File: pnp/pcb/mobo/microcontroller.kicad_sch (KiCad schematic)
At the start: 56 parts, among them J11 XY_LIMIT, J13 HOST, J14 HACK_HEADER, J15 FAN, J17 Z_LIMIT, J2 SWD Header, Q5 AO3400A, Q6 AO3400A, SW1 SW_Push, SW2 SW_Push, U1 STM32F407VETx, U23 PESD5V2S2UT, U24 PESD3V3S2UT, U25 PESD3V3S2UT, U26 PESD3V3S2UT, U27 PESD3V3S2UT, Y1 8MHz

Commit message: Capacitor sourcing
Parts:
- C1, C3, C6, C7: value 2u2 -> 2.2u; JLCPCB C49217 -> C377773; LCSC C49217 -> C377773
- C1, C16, C17, C23: LCSC C476766 -> C38141
- C10, C11, C12, C5, C8, C9: LCSC C360619 -> C38141
- C2, C4: JLCPCB C1785 -> C157608; LCSC C525280 -> C157608
- C29: LCSC C476766 -> C38141; now not fitted
- J11: JLCPCB (none) -> C67258; LCSC (none) -> C67258
- J15: JLCPCB (none) -> C64658; LCSC (none) -> C64658
- J2: now not fitted
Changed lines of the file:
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@@
 			(effects
 				(font
-					(size 1 1)
-					(color 223 129 255 1)
+					(size 1.27 1.27)
 				)
 				(hide yes)
@@
 			(effects
 				(font
-					(size 1 1)
-					(color 223 129 255 1)
+					(size 1.27 1.27)
 				)
 				(hide yes)
 			)
 		)
-		(property "Description" ""
+		(property "Description" "test point"
 			(at 199.39 76.2 0)
 			(effects
@@
 			)
 		)
-		(property "LCSC" "C476766"
+		(property "LCSC" "C38141"
 			(at 146.05 77.47 0)
 			(effects
@@
 			)
 		)
-		(property "LCSC" "C360619"
+		(property "LCSC" "C38141"
 			(at 205.74 39.37 0)
 			(effects
@@
 			)
 		)
-		(property "Value" "2u2"
+		(property "Value" "2.2u"
 			(at 162.56 41.91 0)
 			(effects
@@
 			)
 		)
-		(property "JLCPCB" "C49217"
+		(property "JLCPCB" "C377773"
 			(at 161.29 39.37 0)
 			(effects
@@
 			)
 		)
-		(property "LCSC" "C49217"
+		(property "LCSC" "C377773"
 			(at 161.29 39.37 0)
 			(effects
@@
 			)
 		)
-		(property "LCSC" "C476766"
+		(property "LCSC" "C38141"
 			(at 149.225 254.635 0)
 			(effects
@@
 			)
 		)
-		(property "LCSC" "C360619"
+		(property "LCSC" "C38141"
 			(at 223.52 39.37 0)
 			(effects
@@
 			)
 		)
-		(property "Value" "2u2"
+		(property "Value" "2.2u"
 			(at 171.45 41.91 0)
 			(effects
@@
 			)
 		)
-		(property "JLCPCB" "C49217"
+		(property "JLCPCB" "C377773"
 			(at 170.18 39.37 0)
 			(effects
@@
 			)
 		)
-		(property "LCSC" "C49217"
+		(property "LCSC" "C377773"
 			(at 170.18 39.37 0)
 			(effects
@@
 		(in_bom yes)
 		(on_board yes)
-		(dnp no)
+		(dnp yes)
 		(property "Reference" "J2"
 			(at 158.75 123.19 0)
@@
 			(effects
 				(font
-					(size 1 1)
-					(color 223 129 255 1)
+					(size 1.27 1.27)
 				)
 				(hide yes)
@@
 			(effects
 				(font
-					(size 1 1)
-					(color 223 129 255 1)
+					(size 1.27 1.27)
 				)
 				(hide yes)
 			)
 		)
-		(property "Description" ""
+		(property "Description" "test point"
 			(at 152.4 71.12 0)
 			(effects
@@
 			)
 		)
-		(property "LCSC" "C476766"
+		(property "LCSC" "C38141"
 			(at 89.535 255.27 0)
 			(effects
@@
 			)
 		)
+		(property "JLCPCB" "C64658"
+			(at 391.795 208.28 0)
+			(effects
+				(font
+					(size 1.27 1.27)
+				)
+				(hide yes)
+			)
+		)
+		(property "LCSC" "C64658"
+			(at 391.795 208.28 0)
+			(effects
+				(font
+					(size 1.27 1.27)
+				)
+				(hide yes)
+			)
+		)
 		(pin "1"
 		)
@@
 			)
 		)
-		(property "LCSC" "C360619"
+		(property "LCSC" "C38141"
 			(at 196.85 39.37 0)
 			(effects
@@
 			)
 		)
-		(property "JLCPCB" "C1785"
+		(property "JLCPCB" "C157608"
 			(at 30.48 92.71 0)
 			(effects
@@
 			)
 		)
-		(property "LCSC" "C525280"
+		(property "LCSC" "C157608"
 			(at 30.48 92.71 0)
 			(effects
@@
 			)
 		)
-		(property "JLCPCB" "C1785"
+		(property "JLCPCB" "C157608"
 			(at 50.8 92.71 0)
 			(effects
@@
 			)
 		)
-		(property "LCSC" "C525280"
+		(property "LCSC" "C157608"
 			(at 50.8 92.71 0)
 			(effects
@@
 			)
 		)
-		(property "LCSC" "C360619"
+		(property "LCSC" "C38141"
 			(at 214.63 39.37 0)
 			(effects
@@
 			)
 		)
-		(property "Value" "2u2"
+		(property "Value" "2.2u"
 			(at 36.83 67.31 0)
 			(effects
@@
 			)
 		)
-		(property "JLCPCB" "C49217"
+		(property "JLCPCB" "C377773"
 			(at 41.91 64.77 0)
 			(effects
@@
 			)
 		)
-		(property "LCSC" "C49217"
+		(property "LCSC" "C377773"
 			(at 41.91 64.77 0)
 			(effects
@@
 		(in_bom yes)
 		(on_board yes)
-		(dnp no)
+		(dnp yes)
 		(property "Reference" "C29"
 			(at 201.7268 78.8416 0)
@@
 			)
 		)
-		(property "LCSC" "C476766"
+		(property "LCSC" "C38141"
 			(at 199.39 80.01 0)
 			(effects
@@
 			)
 		)
-		(property "LCSC" "C360619"
+		(property "LCSC" "C38141"
 			(at 179.07 39.37 0)
 			(effects
@@
 			)
 		)
-		(property "LCSC" "C360619"
+		(property "LCSC" "C38141"
 			(at 187.96 39.37 0)
 			(effects
@@
 			)
 		)
-		(property "Value" "2u2"
+		(property "Value" "2.2u"
 			(at 46.99 67.31 0)
 			(effects
@@
 			)
 		)
-		(property "JLCPCB" "C49217"
+		(property "JLCPCB" "C377773"
 			(at 52.07 64.77 0)
 			(effects
@@
 			)
 		)
-		(property "LCSC" "C49217"
+		(property "LCSC" "C377773"
 			(at 52.07 64.77 0)
 			(effects
@@
 			)
 		)
-		(property "LCSC" "C476766"
+		(property "LCSC" "C38141"
 			(at 120.015 254.635 0)
 			(effects
@@
 			(effects
 				(font
-					(size 1 1)
-					(color 223 129 255 1)
+					(size 1.27 1.27)
 				)
 				(hide yes)
@@
 			(effects
 				(font
-					(size 1 1)
-					(color 223 129 255 1)
+					(size 1.27 1.27)
 				)
 				(hide yes)
 			)
 		)
-		(property "Description" ""
+		(property "Description" "test point"
 			(at 189.23 134.62 0)
 			(effects
@@
 			)
 		)
+		(property "JLCPCB" "C67258"
+			(at 139.7 225.425 0)
+			(effects
+				(font
+					(size 1.27 1.27)
+				)
+				(hide yes)
+			)
+		)
+		(property "LCSC" "C67258"
+			(at 139.7 225.425 0)
+			(effects
+				(font
+					(size 1.27 1.27)
+				)
+				(hide yes)
+			)
+		)
 		(pin "2"
 		)
@@
 			(effects
 				(font
-					(size 1 1)
-					(color 223 129 255 1)
+					(size 1.27 1.27)
 				)
 				(hide yes)
@@
 			(effects
 				(font
-					(size 1 1)
-					(color 223 129 255 1)
+					(size 1.27 1.27)
 				)
 				(hide yes)
 			)
 		)
-		(property "Description" ""
+		(property "Description" "test point"
 			(at 189.23 137.16 0)
 			(effects

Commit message: Sourcing complete
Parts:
- J11: LCSC C67258 -> C2829152
- J13: JLCPCB (none) -> C2829154; LCSC (none) -> C64659
- J14: now not fitted
- J15: LCSC C64658 -> C2829150
- J17: JLCPCB (none) -> C146056; LCSC (none) -> C2829153
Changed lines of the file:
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@@
 			)
 		)
+		(property "JLCPCB" "C2829154"
+			(at 29.21 224.79 0)
+			(effects
+				(font
+					(size 1.27 1.27)
+				)
+				(hide yes)
+			)
+		)
+		(property "LCSC" "C64659"
+			(at 29.21 224.79 0)
+			(effects
+				(font
+					(size 1.27 1.27)
+				)
+				(hide yes)
+			)
+		)
 		(pin "3"
 		)
@@
 		(in_bom yes)
 		(on_board yes)
-		(dnp no)
+		(dnp yes)
 		(fields_autoplaced yes)
 		(property "Reference" "J14"
@@
 			)
 		)
-		(property "LCSC" "C64658"
+		(property "LCSC" "C2829150"
 			(at 391.795 208.28 0)
 			(effects
@@
 			)
 		)
+		(property "JLCPCB" "C146056"
+			(at 110.49 223.52 0)
+			(effects
+				(font
+					(size 1.27 1.27)
+				)
+				(hide yes)
+			)
+		)
+		(property "LCSC" "C2829153"
+			(at 110.49 223.52 0)
+			(effects
+				(font
+					(size 1.27 1.27)
+				)
+				(hide yes)
+			)
+		)
 		(pin "MP"
 		)
@@
 			)
 		)
-		(property "LCSC" "C67258"
+		(property "LCSC" "C2829152"
 			(at 139.7 225.425 0)
 			(effects

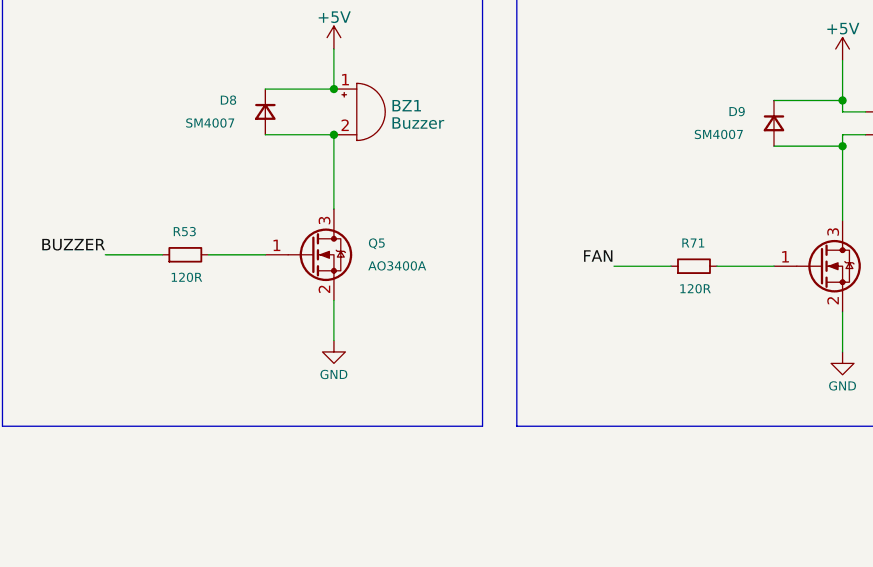
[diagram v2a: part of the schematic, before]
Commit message: Sourcing of resistors complete
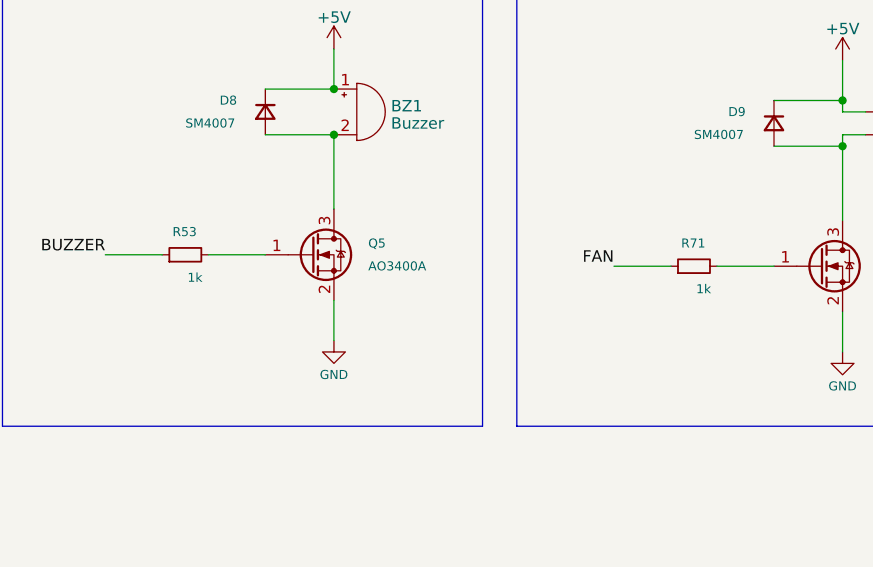
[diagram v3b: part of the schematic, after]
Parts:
- R11, R13, R14: LCSC C17414 -> C115295
- R53, R71: value 120R -> 1k; JLCPCB C17414 -> C17513; LCSC C17414 -> C17513
- R54, R55, R56, R8: JLCPCB C17414 -> C25275; LCSC C17414 -> C25275
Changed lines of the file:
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@@
 			)
 		)
-		(property "LCSC" "C17414"
+		(property "LCSC" "C115295"
 			(at 191.77 80.01 0)
 			(effects
@@
 			)
 		)
-		(property "Value" "120R"
+		(property "Value" "1k"
 			(at 369.57 227.965 90)
 			(effects
@@
 			)
 		)
-		(property "JLCPCB" "C17414"
+		(property "JLCPCB" "C17513"
 			(at 367.665 225.425 0)
 			(effects
@@
 			)
 		)
-		(property "LCSC" "C17414"
+		(property "LCSC" "C17513"
 			(at 367.665 225.425 0)
 			(effects
@@
 			)
 		)
-		(property "JLCPCB" "C17414"
+		(property "JLCPCB" "C25275"
 			(at 363.22 50.8 0)
 			(effects
@@
 			)
 		)
-		(property "LCSC" "C17414"
+		(property "LCSC" "C25275"
 			(at 363.22 50.8 0)
 			(effects
@@
 			)
 		)
-		(property "JLCPCB" "C17414"
+		(property "JLCPCB" "C25275"
 			(at 347.345 44.45 0)
 			(effects
@@
 			)
 		)
-		(property "LCSC" "C17414"
+		(property "LCSC" "C25275"
 			(at 347.345 44.45 0)
 			(effects
@@
 			)
 		)
-		(property "LCSC" "C17414"
+		(property "LCSC" "C115295"
 			(at 177.8 80.01 0)
 			(effects
@@
 			)
 		)
-		(property "LCSC" "C17414"
+		(property "LCSC" "C115295"
 			(at 146.05 67.31 0)
 			(effects
@@
 			)
 		)
-		(property "JLCPCB" "C17414"
+		(property "JLCPCB" "C25275"
 			(at 370.84 53.975 0)
 			(effects
@@
 			)
 		)
-		(property "LCSC" "C17414"
+		(property "LCSC" "C25275"
 			(at 370.84 53.975 0)
 			(effects
@@
 			)
 		)
-		(property "Value" "120R"
+		(property "Value" "1k"
 			(at 313.055 226.695 90)
 			(effects
@@
 			)
 		)
-		(property "JLCPCB" "C17414"
+		(property "JLCPCB" "C17513"
 			(at 311.15 224.155 0)
 			(effects
@@
 			)
 		)
-		(property "LCSC" "C17414"
+		(property "LCSC" "C17513"
 			(at 311.15 224.155 0)
 			(effects
@@
 			)
 		)
-		(property "JLCPCB" "C17414"
+		(property "JLCPCB" "C25275"
 			(at 355.6 47.625 0)
 			(effects
@@
 			)
 		)
-		(property "LCSC" "C17414"
+		(property "LCSC" "C25275"
 			(at 355.6 47.625 0)
 			(effects

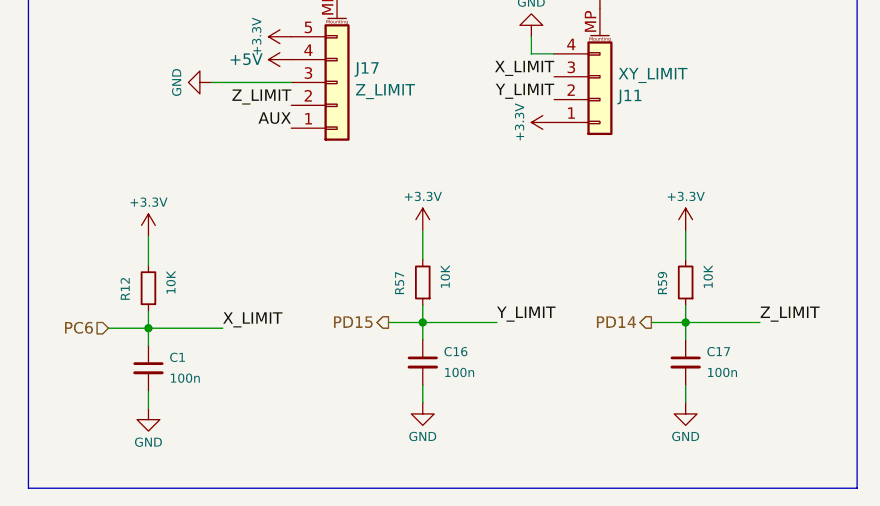
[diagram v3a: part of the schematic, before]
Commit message: Fix part sourcing
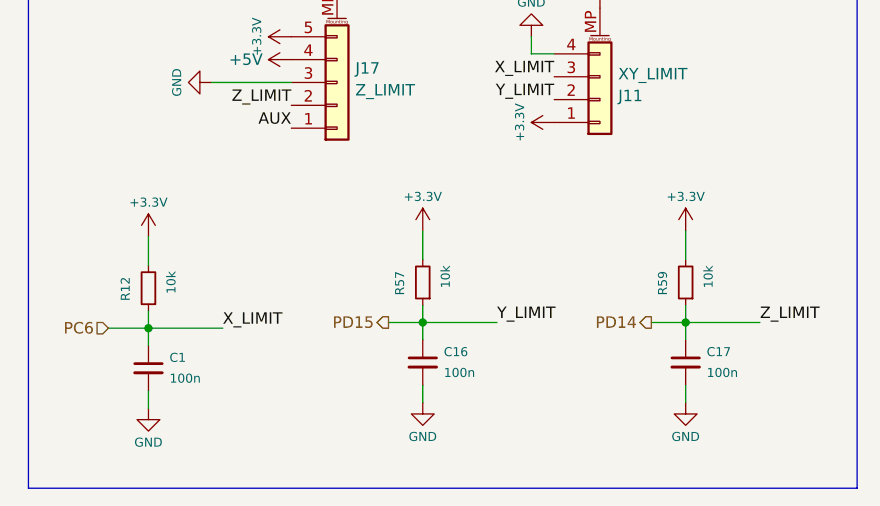
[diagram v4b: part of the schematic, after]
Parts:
- R12, R57, R59: value 10K -> 10k; LCSC C17414 -> C115295
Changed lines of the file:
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@@
 			)
 		)
-		(property "Value" "10K"
+		(property "Value" "10k"
 			(at 151.765 243.84 90)
 			(effects
@@
 			)
 		)
-		(property "LCSC" "C17414"
+		(property "LCSC" "C115295"
 			(at 149.225 245.745 0)
 			(effects
@@
 			)
 		)
-		(property "Value" "10K"
+		(property "Value" "10k"
 			(at 122.555 243.84 90)
 			(effects
@@
 			)
 		)
-		(property "LCSC" "C17414"
+		(property "LCSC" "C115295"
 			(at 120.015 245.745 0)
 			(effects
@@
 			)
 		)
-		(property "Value" "10K"
+		(property "Value" "10k"
 			(at 92.075 244.475 90)
 			(effects
@@
 			)
 		)
-		(property "LCSC" "C17414"
+		(property "LCSC" "C115295"
 			(at 89.535 246.38 0)
 			(effects

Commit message: Change Button PN
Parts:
- SW1, SW2: JLCPCB C720477 -> C455108; LCSC C720477 -> C455108
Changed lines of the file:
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@@
 			)
 		)
-		(property "JLCPCB" "C720477"
+		(property "JLCPCB" "C455108"
 			(at 152.4 77.47 0)
 			(effects
@@
 			)
 		)
-		(property "LCSC" "C720477"
+		(property "LCSC" "C455108"
 			(at 152.4 77.47 0)
 			(effects
@@
 			)
 		)
-		(property "JLCPCB" "C720477"
+		(property "JLCPCB" "C455108"
 			(at 191.77 69.85 0)
 			(effects
@@
 			)
 		)
-		(property "LCSC" "C720477"
+		(property "LCSC" "C455108"
 			(at 191.77 69.85 0)
 			(effects

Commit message: Sourcing of ESD dodes
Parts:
- BZ1: JLCPCB (none) -> C18623826; LCSC (none) -> C18623826
- J14: JLCPCB (none) -> C5383105; LCSC (none) -> C5383105
- U23: JLCPCB (none) -> C2827690; LCSC (none) -> C2827690
- U24, U25, U26, U27: JLCPCB (none) -> C84276; LCSC (none) -> C84276
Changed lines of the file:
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@@
 			)
 		)
+		(property "JLCPCB" "C2827690"
+			(at 328.93 116.205 0)
+			(effects
+				(font
+					(size 1.27 1.27)
+				)
+				(hide yes)
+			)
+		)
+		(property "LCSC" "C2827690"
+			(at 328.93 116.205 0)
+			(effects
+				(font
+					(size 1.27 1.27)
+				)
+				(hide yes)
+			)
+		)
 		(pin "1"
 		)
@@
 			)
 		)
+		(property "JLCPCB" "C84276"
+			(at 358.14 147.32 0)
+			(effects
+				(font
+					(size 1.27 1.27)
+				)
+				(hide yes)
+			)
+		)
+		(property "LCSC" "C84276"
+			(at 358.14 147.32 0)
+			(effects
+				(font
+					(size 1.27 1.27)
+				)
+				(hide yes)
+			)
+		)
 		(pin "1"
 		)
@@
 			)
 		)
+		(property "JLCPCB" "C5383105"
+			(at 225.425 257.175 0)
+			(effects
+				(font
+					(size 1.27 1.27)
+				)
+				(hide yes)
+			)
+		)
+		(property "LCSC" "C5383105"
+			(at 225.425 257.175 0)
+			(effects
+				(font
+					(size 1.27 1.27)
+				)
+				(hide yes)
+			)
+		)
 		(pin "1"
 		)
@@
 			)
 		)
+		(property "JLCPCB" "C84276"
+			(at 358.775 116.205 0)
+			(effects
+				(font
+					(size 1.27 1.27)
+				)
+				(hide yes)
+			)
+		)
+		(property "LCSC" "C84276"
+			(at 358.775 116.205 0)
+			(effects
+				(font
+					(size 1.27 1.27)
+				)
+				(hide yes)
+			)
+		)
 		(pin "1"
 		)
@@
 			)
 		)
+		(property "JLCPCB" "C84276"
+			(at 328.93 147.32 0)
+			(effects
+				(font
+					(size 1.27 1.27)
+				)
+				(hide yes)
+			)
+		)
+		(property "LCSC" "C84276"
+			(at 328.93 147.32 0)
+			(effects
+				(font
+					(size 1.27 1.27)
+				)
+				(hide yes)
+			)
+		)
 		(pin "1"
 		)
@@
 			)
 		)
+		(property "JLCPCB" "C84276"
+			(at 40.005 246.38 0)
+			(effects
+				(font
+					(size 1.27 1.27)
+				)
+				(hide yes)
+			)
+		)
+		(property "LCSC" "C84276"
+			(at 40.005 246.38 0)
+			(effects
+				(font
+					(size 1.27 1.27)
+				)
+				(hide yes)
+			)
+		)
 		(pin "1"
 		)
@@
 			(at 330.2 208.28 0)
 			(effects
+				(font
+					(size 1.27 1.27)
+				)
+				(hide yes)
+			)
+		)
+		(property "JLCPCB" "C18623826"
+			(at 330.2 208.28 0)
+			(effects
+				(font
+					(size 1.27 1.27)
+				)
+				(hide yes)
+			)
+		)
+		(property "LCSC" "C18623826"
+			(at 330.2 208.28 0)
+			(effects

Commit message: rev05 mobo
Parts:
- Q5, Q6: JLCPCB C20917 -> (none); LCSC C427382 -> C347475
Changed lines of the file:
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@@
 			)
 		)
-		(property "JLCPCB" "C20917"
+		(property "JLCPCB" ""
 			(at 381.635 225.425 0)
 			(effects
@@
 			)
 		)
-		(property "LCSC" "C427382"
+		(property "LCSC" "C347475"
 			(at 381.635 225.425 0)
 			(effects
@@
 			)
 		)
-		(property "JLCPCB" "C20917"
+		(property "JLCPCB" ""
 			(at 325.12 224.155 0)
 			(effects
@@
 			)
 		)
-		(property "LCSC" "C427382"
+		(property "LCSC" "C347475"
 			(at 325.12 224.155 0)
 			(effects
